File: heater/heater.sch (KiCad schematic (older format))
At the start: 7 parts, among them J1 power Input, J2 input uC

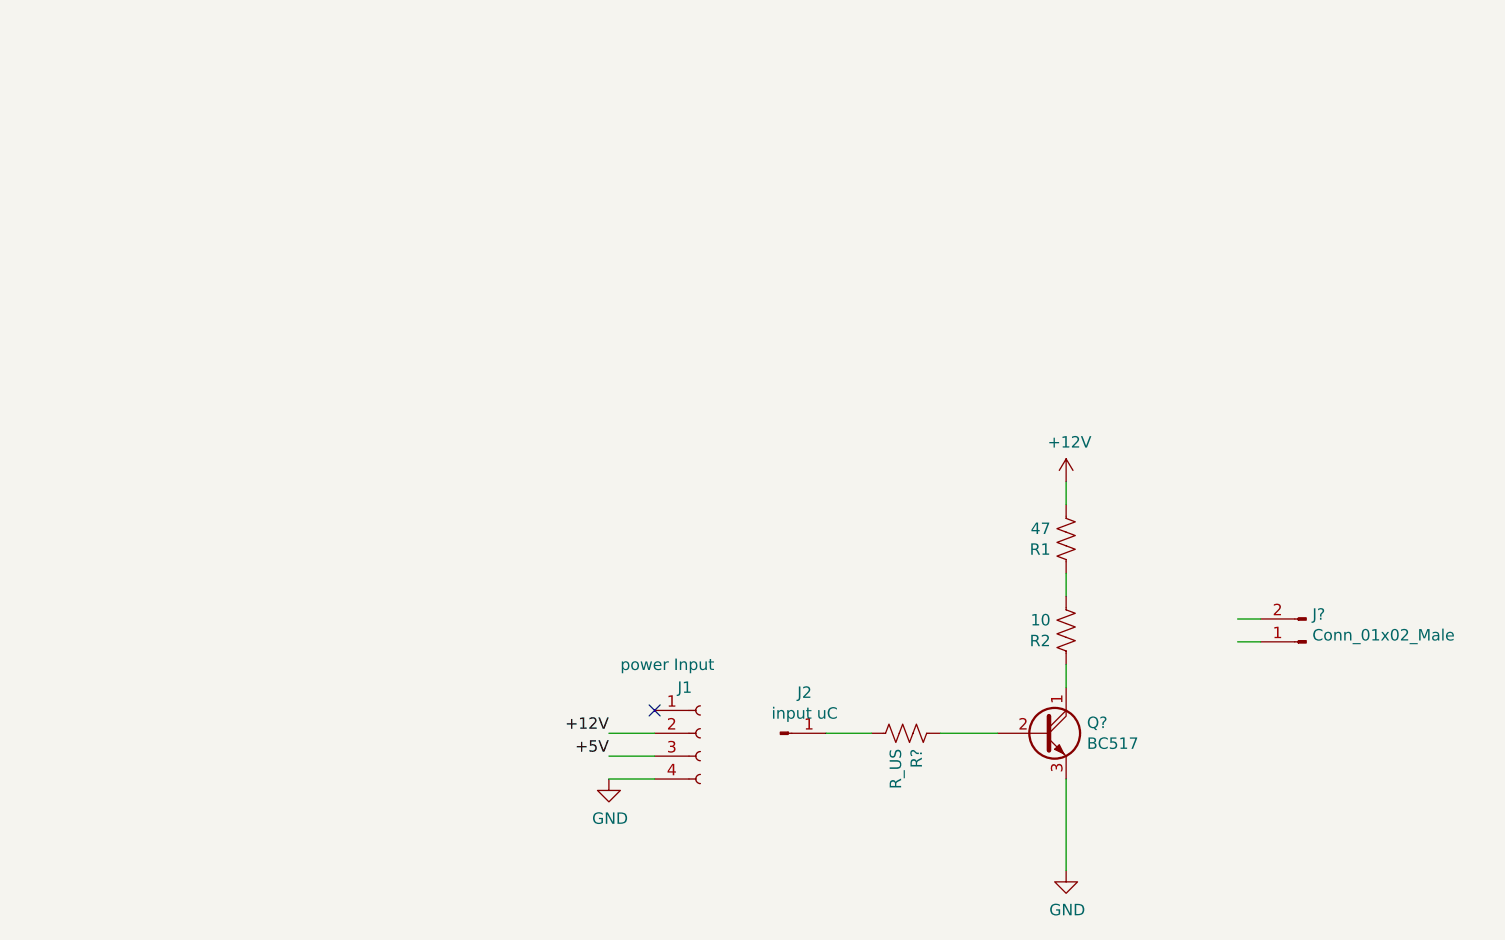
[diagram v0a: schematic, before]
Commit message: Heater major work done; left to design border cuts
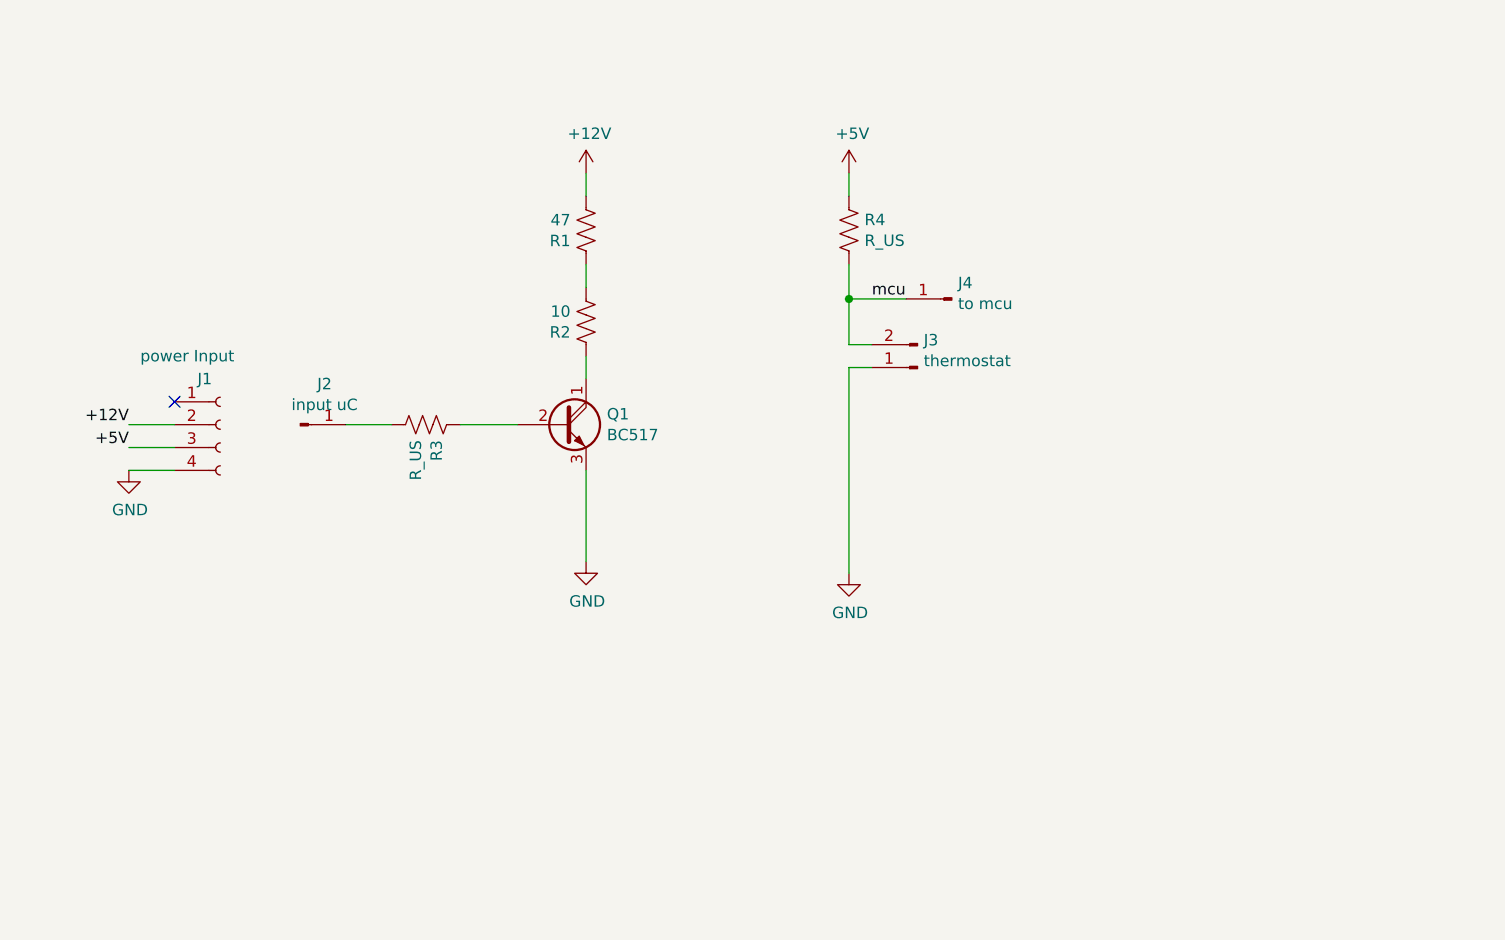
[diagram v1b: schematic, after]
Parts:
- added J4: to mcu, Socket_Strips:Socket_Strip_Straight_1x01_Pitch2.54mm, symbol Connector:Conn_01x01_Male
- added R4: R_US, Resistors_SMD:R_0805_HandSoldering, symbol Device:R_US
- J1: footprint (none) -> Connectors_JST:JST_EH_B04B-EH-A_04x2.50mm_Straight
- J2: footprint (none) -> Socket_Strips:Socket_Strip_Straight_1x01_Pitch2.54mm
- J3: renamed from J?; value Conn_01x02_Male -> thermostat; footprint (none) -> Socket_Strips:Socket_Strip_Straight_1x02_Pitch2.54mm
- Q1: renamed from Q?; footprint Package_TO_SOT_THT:TO-92_Inline -> TO_SOT_Packages_THT:TO-92_Inline_Wide
- R1: footprint (none) -> Resistors_THT:R_Axial_DIN0414_L11.9mm_D4.5mm_P15.24mm_Horizontal
- R2: footprint (none) -> Resistors_THT:R_Axial_Power_L75.0mm_W9.0mm_P81.28mm
- R3: renamed from R?; footprint (none) -> Resistors_SMD:R_0805_HandSoldering
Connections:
- net labels added: mcu
- wire segments 11 -> 16
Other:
- moved on the sheet: J1, J2, J3, Q1, R1, R2, R3
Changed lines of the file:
@@
 EELAYER 26 0
 EELAYER END
-$Descr A 11000 8500
+$Descr User 7874 5906
 encoding utf-8
 Sheet 1 1
@@
 L Device:R_US R2
 U 1 1 5C2F30B4
-P 5850 3400
-F 0 "R2" H 5918 3446 50  0000 L CNN
-F 1 "10" H 5918 3355 50  0000 L CNN
-F 2 "" V 5890 3390 50  0001 C CNN
-F 3 "~" H 5850 3400 50  0001 C CNN
-	1    5850 3400
+P 3750 2050
+F 0 "R2" H 3818 2096 50  0000 L CNN
+F 1 "10" H 3818 2005 50  0000 L CNN
+F 2 "Resistors_THT:R_Axial_Power_L75.0mm_W9.0mm_P81.28mm" V 3790 2040 50  0001 C CNN
+F 3 "~" H 3750 2050 50  0001 C CNN
+	1    3750 2050
 	-1   0    0    1
 $EndComp
@@
 L Device:R_US R1
 U 1 1 5C2F3120
-P 5850 3000
-F 0 "R1" H 5918 3046 50  0000 L CNN
-F 1 "47" H 5918 2955 50  0000 L CNN
-F 2 "" V 5890 2990 50  0001 C CNN
-F 3 "~" H 5850 3000 50  0001 C CNN
-	1    5850 3000
+P 3750 1650
+F 0 "R1" H 3818 1696 50  0000 L CNN
+F 1 "47" H 3818 1605 50  0000 L CNN
+F 2 "Resistors_THT:R_Axial_DIN0414_L11.9mm_D4.5mm_P15.24mm_Horizontal" V 3790 1640 50  0001 C CNN
+F 3 "~" H 3750 1650 50  0001 C CNN
+	1    3750 1650
 	-1   0    0    1
 $EndComp
@@
 L Connector:Conn_01x04_Female J1
 U 1 1 5C2F487D
-P 4250 3850
-F 0 "J1" H 4150 4050 50  0000 L CNN
-F 1 "power Input" H 3900 4150 50  0000 L CNN
-F 2 "" H 4250 3850 50  0001 C CNN
-F 3 "~" H 4250 3850 50  0001 C CNN
-	1    4250 3850
-	1    0    0    -1
-$EndComp
-Wire Wire Line
-	4050 3850 3850 3850
-Wire Wire Line
-	4050 3950 3850 3950
-Wire Wire Line
-	4050 4050 3850 4050
-Text Label 3850 3850 2    50   ~ 0
+P 2150 2500
+F 0 "J1" H 2050 2700 50  0000 L CNN
+F 1 "power Input" H 1800 2800 50  0000 L CNN
+F 2 "Connectors_JST:JST_EH_B04B-EH-A_04x2.50mm_Straight" H 2150 2500 50  0001 C CNN
+F 3 "~" H 2150 2500 50  0001 C CNN
+	1    2150 2500
+	1    0    0    -1
+$EndComp
+Wire Wire Line
+	1950 2500 1750 2500
+Wire Wire Line
+	1950 2600 1750 2600
+Wire Wire Line
+	1950 2700 1750 2700
+Text Label 1750 2500 2    50   ~ 0
 +12V
-Text Label 3850 3950 2    50   ~ 0
+Text Label 1750 2600 2    50   ~ 0
 +5V
 $Comp
-L power:GND #PWR?
+L power:GND #PWR0101
 U 1 1 5C303485
-P 3850 4050
-F 0 "#PWR?" H 3850 3800 50  0001 C CNN
-F 1 "GND" H 3855 3877 50  0000 C CNN
-F 2 "" H 3850 4050 50  0001 C CNN
-F 3 "" H 3850 4050 50  0001 C CNN
-	1    3850 4050
-	1    0    0    -1
-$EndComp
-NoConn ~ 4050 3750
-$Comp
-L Transistor_BJT:BC517 Q?
+P 1750 2700
+F 0 "#PWR0101" H 1750 2450 50  0001 C CNN
+F 1 "GND" H 1755 2527 50  0000 C CNN
+F 2 "" H 1750 2700 50  0001 C CNN
+F 3 "" H 1750 2700 50  0001 C CNN
+	1    1750 2700
+	1    0    0    -1
+$EndComp
+NoConn ~ 1950 2400
+$Comp
+L Transistor_BJT:BC517 Q1
 U 1 1 5C303654
-P 5750 3850
-F 0 "Q?" H 5941 3896 50  0000 L CNN
-F 1 "BC517" H 5941 3805 50  0000 L CNN
-F 2 "Package_TO_SOT_THT:TO-92_Inline" H 5950 3775 50  0001 L CIN
-F 3 "http://www.fairchildsemi.com/ds/BC/BC517.pdf" H 5750 3850 50  0001 L CNN
-	1    5750 3850
+P 3650 2500
+F 0 "Q1" H 3841 2546 50  0000 L CNN
+F 1 "BC517" H 3841 2455 50  0000 L CNN
+F 2 "TO_SOT_Packages_THT:TO-92_Inline_Wide" H 3850 2425 50  0001 L CIN
+F 3 "http://www.fairchildsemi.com/ds/BC/BC517.pdf" H 3650 2500 50  0001 L CNN
+	1    3650 2500
 	1    0    0    -1
 $EndComp
@@
 L Connector:Conn_01x01_Male J2
 U 1 1 5C307D7B
-P 4600 3850
-F 0 "J2" H 4706 4028 50  0000 C CNN
-F 1 "input uC" H 4706 3937 50  0000 C CNN
-F 2 "" H 4600 3850 50  0001 C CNN
-F 3 "~" H 4600 3850 50  0001 C CNN
-	1    4600 3850
-	1    0    0    -1
-$EndComp
-$Comp
-L Device:R_US R?
+P 2500 2500
+F 0 "J2" H 2606 2678 50  0000 C CNN
+F 1 "input uC" H 2606 2587 50  0000 C CNN
+F 2 "Socket_Strips:Socket_Strip_Straight_1x01_Pitch2.54mm" H 2500 2500 50  0001 C CNN
+F 3 "~" H 2500 2500 50  0001 C CNN
+	1    2500 2500
+	1    0    0    -1
+$EndComp
+$Comp
+L Device:R_US R3
 U 1 1 5C307DD4
-P 5150 3850
-F 0 "R?" H 5218 3896 50  0000 L CNN
-F 1 "R_US" H 5218 3805 50  0000 L CNN
-F 2 "" V 5190 3840 50  0001 C CNN
-F 3 "~" H 5150 3850 50  0001 C CNN
-	1    5150 3850
+P 3050 2500
+F 0 "R3" H 3118 2546 50  0000 L CNN
+F 1 "R_US" H 3118 2455 50  0000 L CNN
+F 2 "Resistors_SMD:R_0805_HandSoldering" V 3090 2490 50  0001 C CNN
+F 3 "~" H 3050 2500 50  0001 C CNN
+	1    3050 2500
 	0    1    1    0
 $EndComp
 Wire Wire Line
-	4800 3850 5000 3850
-Wire Wire Line
-	5300 3850 5550 3850
-Wire Wire Line
-	5850 3150 5850 3250
-Wire Wire Line
-	5850 3550 5850 3650
-Wire Wire Line
-	5850 2850 5850 2750
-$Comp
-L power:+12V #PWR?
+	2700 2500 2900 2500
+Wire Wire Line
+	3200 2500 3450 2500
+Wire Wire Line
+	3750 1800 3750 1900
+Wire Wire Line
+	3750 2200 3750 2300
+Wire Wire Line
+	3750 1500 3750 1400
+$Comp
+L power:+12V #PWR0102
 U 1 1 5C3081C8
-P 5850 2750
-F 0 "#PWR?" H 5850 2600 50  0001 C CNN
-F 1 "+12V" H 5865 2923 50  0000 C CNN
-F 2 "" H 5850 2750 50  0001 C CNN
-F 3 "" H 5850 2750 50  0001 C CNN
-	1    5850 2750
-	1    0    0    -1
-$EndComp
-Wire Wire Line
-	5850 4050 5850 4450
-$Comp
-L power:GND #PWR?
+P 3750 1400
+F 0 "#PWR0102" H 3750 1250 50  0001 C CNN
+F 1 "+12V" H 3765 1573 50  0000 C CNN
+F 2 "" H 3750 1400 50  0001 C CNN
+F 3 "" H 3750 1400 50  0001 C CNN
+	1    3750 1400
+	1    0    0    -1
+$EndComp
+Wire Wire Line
+	3750 2700 3750 3100
+$Comp
+L power:GND #PWR0103
 U 1 1 5C308243
-P 5850 4450
-F 0 "#PWR?" H 5850 4200 50  0001 C CNN
-F 1 "GND" H 5855 4277 50  0000 C CNN
-F 2 "" H 5850 4450 50  0001 C CNN
-F 3 "" H 5850 4450 50  0001 C CNN
-	1    5850 4450
-	1    0    0    -1
-$EndComp
-$Comp
-L Connector:Conn_01x02_Male J?
+P 3750 3100
+F 0 "#PWR0103" H 3750 2850 50  0001 C CNN
+F 1 "GND" H 3755 2927 50  0000 C CNN
+F 2 "" H 3750 3100 50  0001 C CNN
+F 3 "" H 3750 3100 50  0001 C CNN
+	1    3750 3100
+	1    0    0    -1
+$EndComp
+$Comp
+L Connector:Conn_01x02_Male J3
 U 1 1 5C308B5A
-P 6900 3450
-F 0 "J?" H 6873 3330 50  0000 R CNN
-F 1 "Conn_01x02_Male" H 6873 3421 50  0000 R CNN
-F 2 "" H 6900 3450 50  0001 C CNN
-F 3 "~" H 6900 3450 50  0001 C CNN
-	1    6900 3450
-	-1   0    0    1
-$EndComp
-Wire Wire Line
-	6700 3350 6600 3350
-Wire Wire Line
-	6700 3450 6600 3450
+P 5200 2250
+F 0 "J3" H 5173 2130 50  0000 R CNN
+F 1 "thermostat" H 5173 2221 50  0000 R CNN
+F 2 "Socket_Strips:Socket_Strip_Straight_1x02_Pitch2.54mm" H 5200 2250 50  0001 C CNN
+F 3 "~" H 5200 2250 50  0001 C CNN
+	1    5200 2250
+	-1   0    0    1
+$EndComp
+Wire Wire Line
+	5000 2250 4900 2250
+$Comp
+L Device:R_US R4
+U 1 1 5C336026
+P 4900 1650
+F 0 "R4" H 4968 1696 50  0000 L CNN
+F 1 "R_US" H 4968 1605 50  0000 L CNN
+F 2 "Resistors_SMD:R_0805_HandSoldering" V 4940 1640 50  0001 C CNN
+F 3 "~" H 4900 1650 50  0001 C CNN
+	1    4900 1650
+	1    0    0    -1
+$EndComp
+$Comp
+L power:GND #PWR0104
+U 1 1 5C3360BC
+P 4900 3150
+F 0 "#PWR0104" H 4900 2900 50  0001 C CNN
+F 1 "GND" H 4905 2977 50  0000 C CNN
+F 2 "" H 4900 3150 50  0001 C CNN
+F 3 "" H 4900 3150 50  0001 C CNN
+	1    4900 3150
+	1    0    0    -1
+$EndComp
+Wire Wire Line
+	5000 2150 4900 2150
+Wire Wire Line
+	4900 2150 4900 1950
+Wire Wire Line
+	4900 2250 4900 3150
+$Comp
+L power:+5V #PWR0105
+U 1 1 5C33660C
+P 4900 1400
+F 0 "#PWR0105" H 4900 1250 50  0001 C CNN
+F 1 "+5V" H 4915 1573 50  0000 C CNN
+F 2 "" H 4900 1400 50  0001 C CNN
+F 3 "" H 4900 1400 50  0001 C CNN
+	1    4900 1400
+	1    0    0    -1
+$EndComp
+Wire Wire Line
+	4900 1400 4900 1500
+Wire Wire Line
+	4900 1950 5150 1950
+Connection ~ 4900 1950
+Wire Wire Line
+	4900 1950 4900 1800
+Text Label 5000 1950 0    50   ~ 0
+mcu
+$Comp
+L Connector:Conn_01x01_Male J4
+U 1 1 5C336DF5
+P 5350 1950
+F 0 "J4" H 5323 1880 50  0000 R CNN
+F 1 "to mcu" H 5323 1971 50  0000 R CNN
+F 2 "Socket_Strips:Socket_Strip_Straight_1x01_Pitch2.54mm" H 5350 1950 50  0001 C CNN
+F 3 "~" H 5350 1950 50  0001 C CNN
+	1    5350 1950
+	-1   0    0    1
+$EndComp
 $EndSCHEMATC
